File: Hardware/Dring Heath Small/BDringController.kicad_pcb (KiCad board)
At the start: 2 copper layers, 144.8 x 131.4 mm, 97 parts, among them J1 AUX GPIO, J10 Module 2, J11 VMot, J12 Module 3, J13 Shift Regs and Motor Drvs, J14 Module 4, J15 Module 5, J16 Micro_SD_Card, J17 Pin, J18 Pin, J19 Pin, J20 Pin, J21 Pin, J22 Pin, J3 Module 1, J4 Jumper, J5 Motor, J6 Module 1, J7 Ext Mot Drv, J8 01x02, J9 THC_Display, U1 ESP32_38p, U10 Y, U11 z, U12 A, U13 B, U14 C, U2 74LVC157A, U3 ESP32_38p, U4 BL8071CLATR33, U5 74AHCT595, U6 74AHCT595, U7 74AHCT595, U8 74AHCT595, U9 X

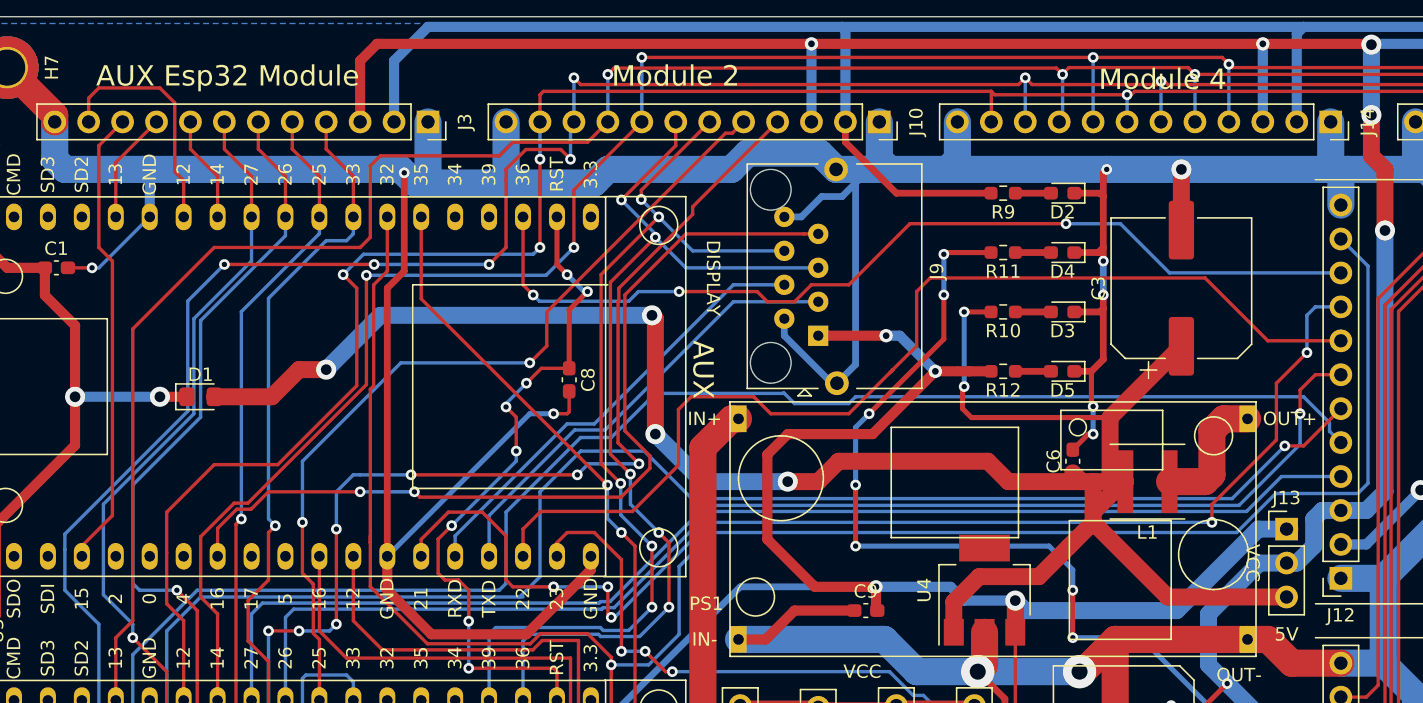
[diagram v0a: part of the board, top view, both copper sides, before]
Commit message: routed a/d board
put simulation on excel bom
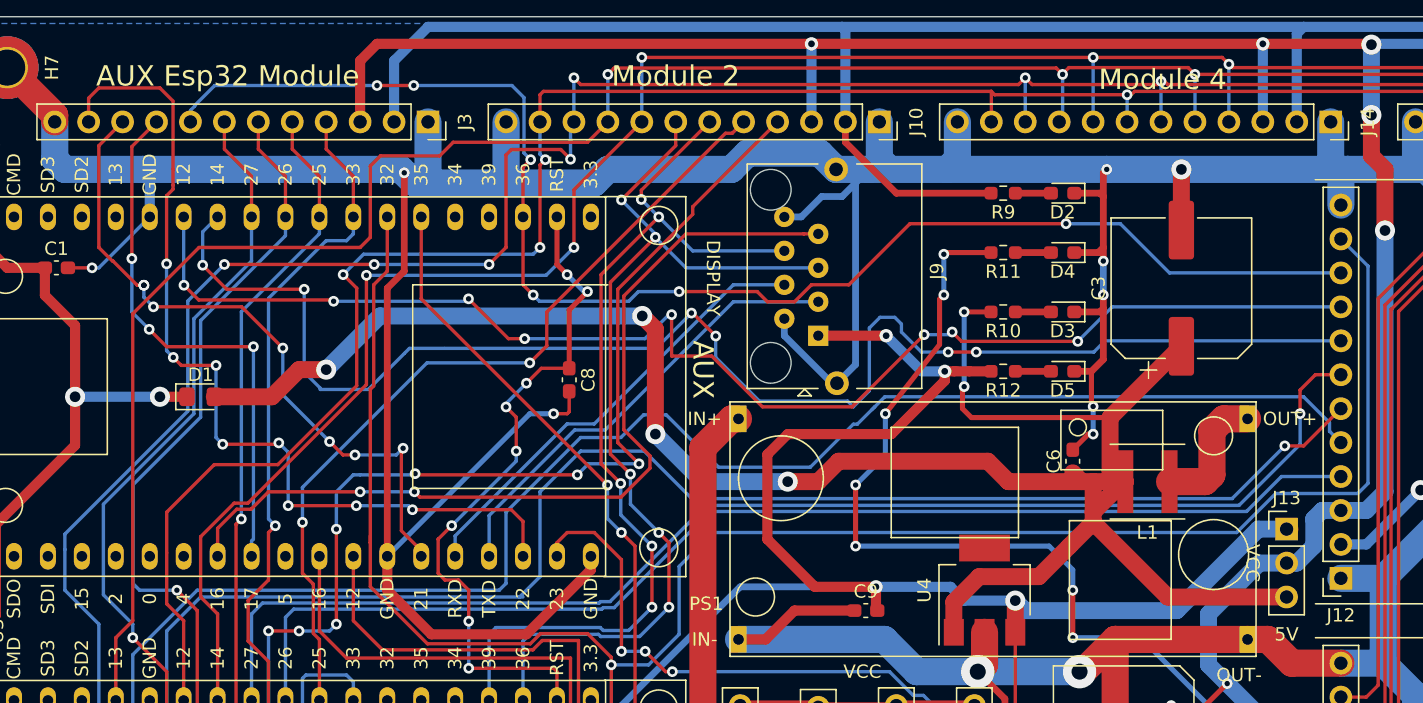
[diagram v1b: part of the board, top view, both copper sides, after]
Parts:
- J3: value Module 1 -> Torch module
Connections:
- J12 pad 8: TCHIO22 -> Ready
- J12 pad 9: TCHIO21 -> Handover
- J3 pad 8: Net-(J3-Pad8) -> TCH_V_IO36
- U1 pad 14: TCHIO21 -> Net-(J3-Pad10)
- U1 pad 17: TCHIO22 -> Net-(J3-Pad11)
- U1 pad 31: Net-(J3-Pad8) -> Ready
- U1 pad 32: Net-(J3-Pad11) -> Handover
- U1 pad 34: Net-(J3-Pad9) -> Net-(U1-Pad34)
- U1 pad 4: Net-(J3-Pad10) -> Net-(U1-Pad4)
- U1 pad 9: Net-(U1-Pad9) -> Net-(J3-Pad9)
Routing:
- net Ready: track 0.00 -> 110.3 mm, vias 0 -> 6
- net Handover: track 0.00 -> 102.6 mm, vias 0 -> 8
- net TCHIO21: track 91.9 -> 0.00 mm, vias 5 -> 0
- net TCHIO22: track 79.2 -> 0.00 mm
- net Net-(J3-Pad11): track 17.8 -> 67.9 mm, vias 0 -> 8
- net TCH_V_IO36: track 71.4 -> 107.7 mm, vias 3 -> 6
- net Net-(J3-Pad9): track 8.37 -> 40.9 mm, vias 0 -> 3
- net Net-(J3-Pad10): track 34.6 -> 50.9 mm, vias 0 -> 7
- net Net-(J3-Pad8): track 7.95 -> 0.00 mm
- net GPIO04: track 134.5 -> 137.3 mm
- net GPIO25: track 63.5 -> 62.3 mm
- net +3V3: track 185.4 -> 186.5 mm
- net Net-(U1-Pad4): track 0.00 -> 0.76 mm
- net GPIO13: track 210.2 -> 210.9 mm
- net GPIO15: track 238.1 -> 238.7 mm

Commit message: changed reset circuit on ESP 32s and driver board gerber
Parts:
- removed C8: 10uf, Capacitor_SMD:C_0603_1608Metric_Pad1.08x0.95mm_HandSolder
- added J23: RST, Connector_PinHeader_2.54mm:PinHeader_1x02_P2.54mm_Vertical, F.Cu at (97.3, 29.0)
- added J24: RST, Connector_PinHeader_2.54mm:PinHeader_1x02_P2.54mm_Vertical, F.Cu at (103.7, 29.1)
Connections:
- U1 pad 21: EN -> Net-(J23-Pad1)
- U3 pad 21: EN -> Net-(J24-Pad1)
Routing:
- net Net-(J24-Pad1): track 0.00 -> 62.0 mm, vias 0 -> 6
- net EN: track 51.8 -> 0.00 mm, vias 8 -> 0
- net Net-(J23-Pad1): track 0.00 -> 23.8 mm, vias 0 -> 3
- net GND: track 1015.7 -> 1008.7 mm, vias 51 -> 50
- net GPIO12: track 191.1 -> 189.9 mm
- net GPIO15: track 238.7 -> 238.0 mm
- net Net-(J3-Pad10): track 50.9 -> 50.2 mm
